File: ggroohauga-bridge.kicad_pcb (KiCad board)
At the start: 2 copper layers, 101.6 x 31 mm, 6 parts

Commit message: Move stuff around
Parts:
- moved C-Q1 6.23 mm to (135.7, 59.4)
- moved A-R1 4.06 mm to (74.7, 73.2)
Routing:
- net /GPIO_L40_C40_M41/CON_POWER_OUT: track 32.1 -> 38.5 mm
- net /CON_POWER_OUT: track 18.1 -> 11.9 mm
- net +3.3V: track 64.4 -> 70.6 mm
- net /AMP_POWER_IN: track 18.3 -> 14.0 mm
- net /GPIO_L8_C8_M10/AMP_POWER_IN: track 31.7 -> 36.0 mm
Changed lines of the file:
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@@
 	(footprint "Package_TO_SOT_SMD:SOT-23"
 		(layer "F.Cu")
-		(at 129.474 59.3575 -90)
+		(at 135.702 59.3575 -90)
 		(descr "SOT, 3 Pin (JEDEC TO-236 Var AB https://www.jedec.org/document_search?search_api_views_fulltext=TO-236), generated with kicad-footprint-generator ipc_gullwing_generator.py")
 		(tags "SOT TO_SOT_SMD")
 		(property "Reference" "C-Q1"
-			(at 1.0945 3.998 180)
+			(at -2.9695 0.066 180)
 			(layer "F.SilkS")
 			(effects
@@
 	(footprint "Resistor_SMD:R_0805_2012Metric_Pad1.20x1.40mm_HandSolder"
 		(layer "F.Cu")
-		(at 78.724 72.644 180)
+		(at 74.692 73.152 180)
 		(descr "Resistor SMD 0805 (2012 Metric), square (rectangular) end terminal, IPC_7351 nominal with elongated pad for handsoldering. (Body size source: IPC-SM-782 page 72, https://www.pcb-3d.com/wordpress/wp-content/uploads/ipc-sm-782a_amendment_1_and_2.pdf), generated with kicad-footprint-generator")
 		(tags "resistor handsolder")
@@
 	)
 	(segment
-		(start 74.168 73.66)
-		(end 63.5 73.66)
+		(start 62.8396 72.9996)
+		(end 62.8396 70.3192)
 		(width 0.2)
 		(layer "F.Cu")
@@
 	)
 	(segment
-		(start 77.724 72.644)
-		(end 75.184 72.644)
+		(start 71.12 73.152)
+		(end 73.692 73.152)
 		(width 0.2)
 		(layer "F.Cu")
@@
 	)
 	(segment
-		(start 75.184 72.644)
-		(end 74.168 73.66)
+		(start 63.5 73.66)
+		(end 70.612 73.66)
 		(width 0.2)
 		(layer "F.Cu")
@@
 	)
 	(segment
-		(start 62.8396 72.9996)
-		(end 62.8396 70.3192)
+		(start 63.5 73.66)
+		(end 62.8396 72.9996)
 		(width 0.2)
 		(layer "F.Cu")
@@
 	)
 	(segment
-		(start 63.5 73.66)
-		(end 62.8396 72.9996)
+		(start 70.612 73.66)
+		(end 71.12 73.152)
 		(width 0.2)
 		(layer "F.Cu")
@@
 	)
 	(segment
+		(start 79.724 72.644)
+		(end 79.216 73.152)
+		(width 0.2)
+		(layer "F.Cu")
+		(net 16)
+	)
+	(segment
 		(start 109.474 77.47)
 		(end 106.172 74.168)
@@
 	)
 	(segment
+		(start 79.216 73.152)
+		(end 75.692 73.152)
+		(width 0.2)
+		(layer "F.Cu")
+		(net 16)
+	)
+	(segment
 		(start 106.172 74.168)
 		(end 96.774 74.168)
@@
 	)
 	(segment
-		(start 124.46 72.644)
-		(end 129.474 72.644)
+		(start 135.636 72.644)
+		(end 124.46 72.644)
 		(width 0.2)
 		(layer "F.Cu")
@@
 	)
 	(segment
-		(start 83.312 73.66)
-		(end 81.788 73.66)
+		(start 135.702 60.295)
+		(end 135.702 72.578)
 		(width 0.2)
 		(layer "F.Cu")
@@
 	)
 	(segment
-		(start 81.534 73.914)
-		(end 81.534 77.47)
+		(start 135.702 72.578)
+		(end 135.636 72.644)
+		(width 0.2)
+		(layer "F.Cu")
+		(net 21)
+	)
+	(segment
+		(start 83.312 73.66)
+		(end 81.788 73.66)
 		(width 0.2)
 		(layer "F.Cu")
@@
 	)
 	(segment
-		(start 129.474 72.644)
-		(end 129.474 60.295)
+		(start 81.534 73.914)
+		(end 81.534 77.47)
 		(width 0.2)
 		(layer "F.Cu")
@@
 	)
 	(segment
-		(start 123.952 57.912)
-		(end 124.018 57.978)
-		(width 0.2)
-		(layer "F.Cu")
-		(net 22)
-	)
-	(segment
-		(start 124.018 57.978)
-		(end 128.524 57.978)
+		(start 124.46 58.42)
+		(end 134.752 58.42)
 		(width 0.2)
 		(layer "F.Cu")
@@
 	)
 	(via
-		(at 123.952 57.912)
+		(at 124.46 58.42)
 		(size 0.6)
 		(drill 0.3)
@@
 	)
 	(segment
-		(start 99.314 57.15)
-		(end 99.314 54.61)
+		(start 99.568 57.404)
+		(end 99.314 57.15)
 		(width 0.2)
 		(layer "B.Cu")
@@
 	)
 	(segment
-		(start 99.568 57.404)
-		(end 99.314 57.15)
+		(start 124.46 58.42)
+		(end 123.444 57.404)
 		(width 0.2)
 		(layer "B.Cu")
@@
 	)
 	(segment
-		(start 123.952 57.912)
-		(end 123.444 57.404)
+		(start 99.314 57.15)
+		(end 99.314 54.61)
 		(width 0.2)
 		(layer "B.Cu")
@@
 	(segment
 		(start 144.487759 58.42)
-		(end 146.5072 60.439441)
+		(end 136.652 58.42)
 		(width 0.2)
 		(layer "F.Cu")
@@
 	)
 	(segment
-		(start 130.424 58.42)
-		(end 144.487759 58.42)
+		(start 146.5072 61.6592)
+		(end 146.5072 60.439441)
 		(width 0.2)
 		(layer "F.Cu")
@@
 	(segment
 		(start 146.5072 60.439441)
-		(end 146.5072 61.6592)
+		(end 144.487759 58.42)
 		(width 0.2)
 		(layer "F.Cu")

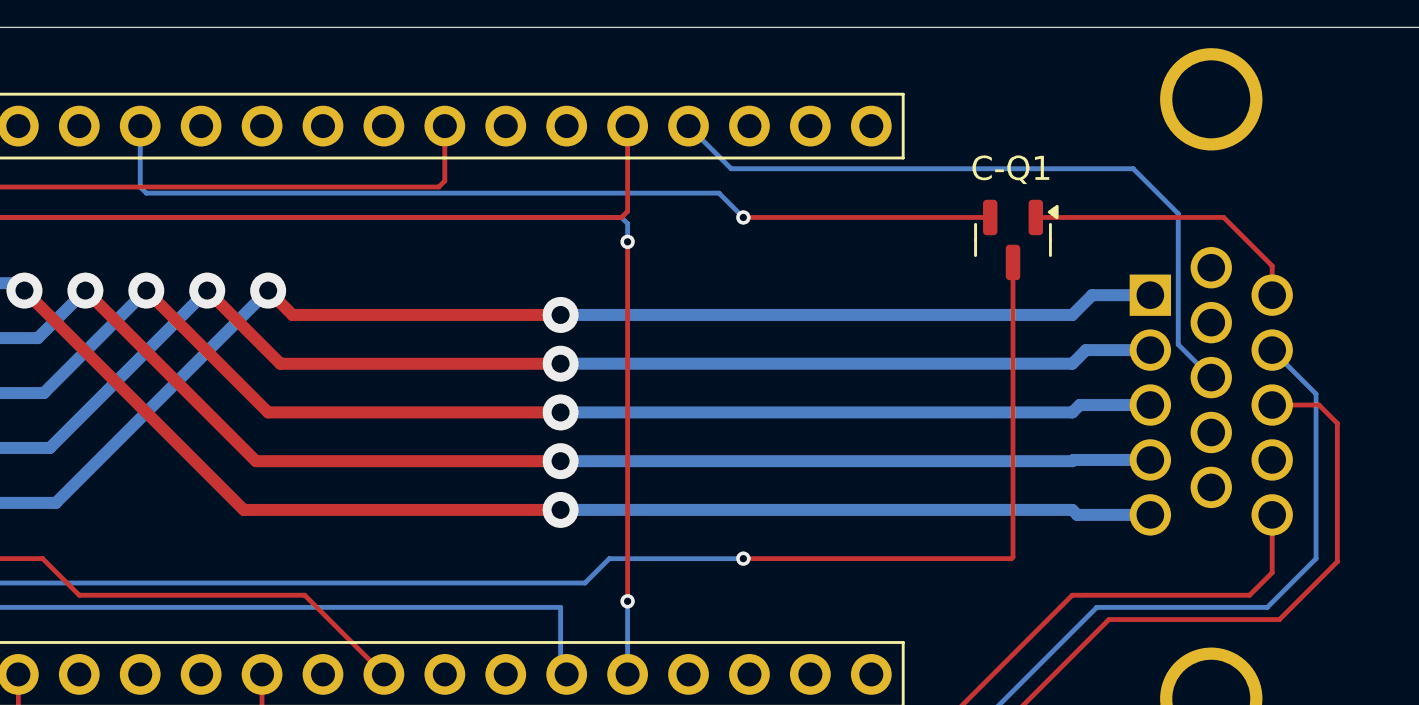
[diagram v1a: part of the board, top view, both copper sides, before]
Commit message: Rotate MOSFET pins so that it's connected correctly
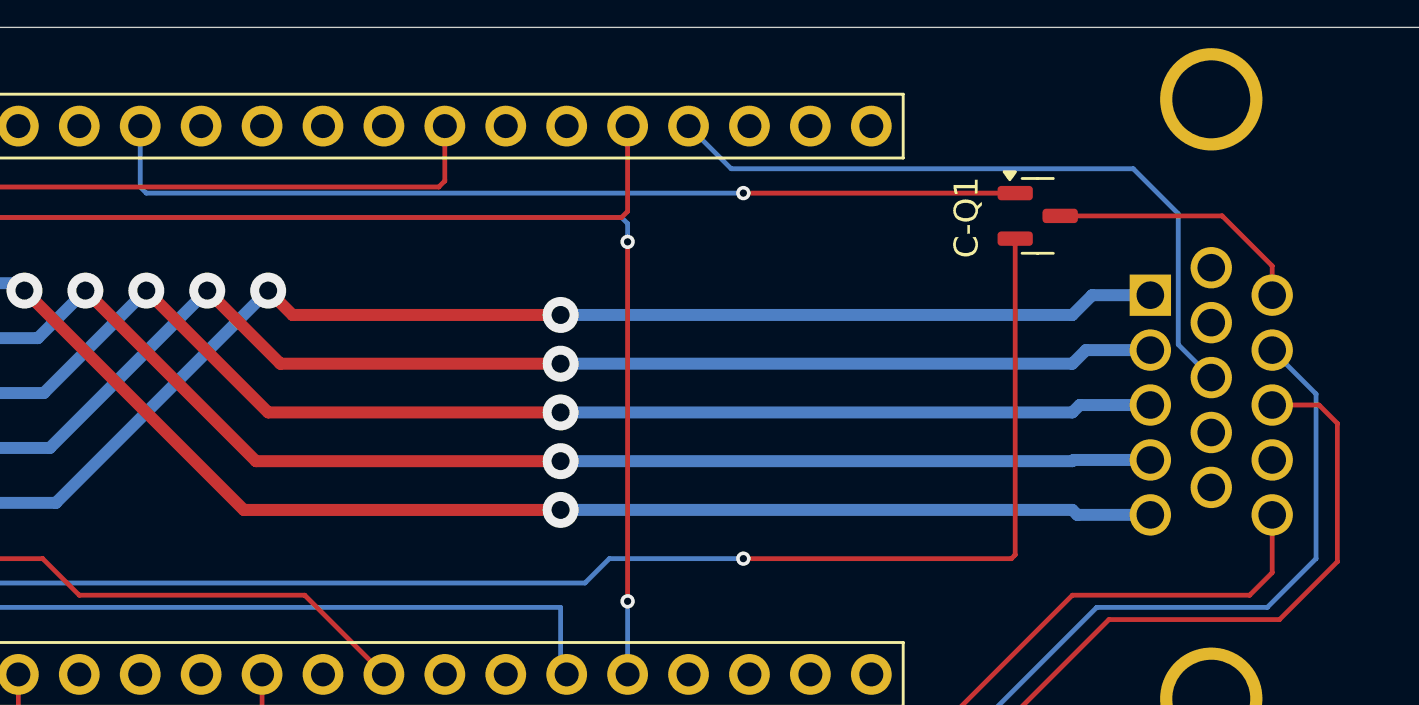
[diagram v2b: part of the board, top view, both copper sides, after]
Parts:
- moved C-Q1 1.44 mm to (136.7, 58.4), turned to 0 degrees
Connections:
- A-J1 pad S1: (no net) -> GND
- A-J1 pad S2: (no net) -> GND
- C-J1 pad SH1: (no net) -> GND
- C-J1 pad SH2: (no net) -> GND
- C-Q1 pad 1: /CON_POWER_OUT -> /GPIO_L40_C40_M41/CON_POWER_OUT
- C-Q1 pad 2: /GPIO_L40_C40_M41/CON_POWER_OUT -> +3.3V
- C-Q1 pad 3: +3.3V -> /CON_POWER_OUT
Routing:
- net +3.3V: track 70.6 -> 71.6 mm
- net /CON_POWER_OUT: track 11.9 -> 10.9 mm
- net /GPIO_L40_C40_M41/CON_POWER_OUT: track 38.5 -> 39.1 mm
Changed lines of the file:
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@@
 	(footprint "Package_TO_SOT_SMD:SOT-23"
 		(layer "F.Cu")
-		(at 135.702 59.3575 -90)
+		(at 136.7305 58.354)
 		(descr "SOT, 3 Pin (JEDEC TO-236 Var AB https://www.jedec.org/document_search?search_api_views_fulltext=TO-236), generated with kicad-footprint-generator ipc_gullwing_generator.py")
 		(tags "SOT TO_SOT_SMD")
 		(property "Reference" "C-Q1"
-			(at -2.9695 0.066 180)
+			(at -2.9695 0.066 90)
 			(layer "F.SilkS")
 			(effects
@@
 		)
 		(property "Value" "DMP2004K"
-			(at 0 2.4 90)
+			(at 0 2.4 0)
 			(layer "F.Fab")
 			(effects
@@
 		)
 		(property "Footprint" "Package_TO_SOT_SMD:SOT-23"
-			(at 0 0 90)
+			(at 0 0 0)
 			(layer "F.Fab")
 			(hide yes)
@@
 		)
 		(property "Datasheet" "https://www.diodes.com/assets/Datasheets/DMP2004K.pdf"
-			(at 0 0 90)
+			(at 0 0 0)
 			(layer "F.Fab")
 			(hide yes)
@@
 		)
 		(property "Description" "-600mA Id, -20V Vds, P-Channel MOSFET, SOT-23"
-			(at 0 0 90)
+			(at 0 0 0)
 			(layer "F.Fab")
 			(hide yes)
@@
 		)
 		(property "Sim.Device" "PMOS"
-			(at 0 0 -90)
+			(at 0 0 0)
 			(unlocked yes)
 			(layer "F.Fab")
@@
 		)
 		(property "Sim.Type" "VDMOS"
-			(at 0 0 -90)
+			(at 0 0 0)
 			(unlocked yes)
 			(layer "F.Fab")
@@
 			)
 		)
-		(property "Sim.Pins" "1=D 2=G 3=S"
-			(at 0 0 -90)
+		(property "Sim.Pins" "1=G 2=S 3=D"
+			(at 0 0 0)
 			(unlocked yes)
 			(layer "F.Fab")
@@
 		(attr smd)
 		(fp_line
-			(start 0 1.56)
-			(end -0.65 1.56)
+			(start 0 -1.56)
+			(end -0.65 -1.56)
 			(stroke
 				(width 0.12)
@@
 		)
 		(fp_line
-			(start 0 1.56)
-			(end 0.65 1.56)
+			(start 0 -1.56)
+			(end 0.65 -1.56)
 			(stroke
 				(width 0.12)
@@
 		)
 		(fp_line
-			(start 0 -1.56)
-			(end -0.65 -1.56)
+			(start 0 1.56)
+			(end -0.65 1.56)
 			(stroke
 				(width 0.12)
@@
 		)
 		(fp_line
-			(start 0 -1.56)
-			(end 0.65 -1.56)
+			(start 0 1.56)
+			(end 0.65 1.56)
 			(stroke
 				(width 0.12)
@@
 		)
 		(fp_line
-			(start -1.92 1.7)
-			(end 1.92 1.7)
+			(start -1.92 -1.7)
+			(end -1.92 1.7)
 			(stroke
 				(width 0.05)
@@
 		)
 		(fp_line
-			(start 1.92 1.7)
-			(end 1.92 -1.7)
+			(start -1.92 1.7)
+			(end 1.92 1.7)
 			(stroke
 				(width 0.05)
@@
 		)
 		(fp_line
-			(start -1.92 -1.7)
-			(end -1.92 1.7)
+			(start 1.92 -1.7)
+			(end -1.92 -1.7)
 			(stroke
 				(width 0.05)
@@
 		)
 		(fp_line
-			(start 1.92 -1.7)
-			(end -1.92 -1.7)
+			(start 1.92 1.7)
+			(end 1.92 -1.7)
 			(stroke
 				(width 0.05)
@@
 		)
 		(fp_line
-			(start -0.65 1.45)
-			(end -0.65 -1.125)
+			(start -0.65 -1.125)
+			(end -0.325 -1.45)
 			(stroke
 				(width 0.1)
@@
 		)
 		(fp_line
-			(start 0.65 1.45)
-			(end -0.65 1.45)
+			(start -0.65 1.45)
+			(end -0.65 -1.125)
 			(stroke
 				(width 0.1)
@@
 		)
 		(fp_line
-			(start -0.65 -1.125)
-			(end -0.325 -1.45)
+			(start -0.325 -1.45)
+			(end 0.65 -1.45)
 			(stroke
 				(width 0.1)
@@
 		)
 		(fp_line
-			(start -0.325 -1.45)
-			(end 0.65 -1.45)
+			(start 0.65 -1.45)
+			(end 0.65 1.45)
 			(stroke
 				(width 0.1)
@@
 		)
 		(fp_line
-			(start 0.65 -1.45)
-			(end 0.65 1.45)
+			(start 0.65 1.45)
+			(end -0.65 1.45)
 			(stroke
 				(width 0.1)
@@
 		)
 		(fp_text user "${REFERENCE}"
-			(at 0 0 90)
+			(at 0 0 0)
 			(layer "F.Fab")
 			(effects
@@
 		)
 		(pad "1" smd roundrect
-			(at -0.9375 -0.95 270)
+			(at -0.9375 -0.95)
 			(size 1.475 0.6)
 			(layers "F.Cu" "F.Paste" "F.Mask")
 			(roundrect_rratio 0.25)
-			(net 52 "/CON_POWER_OUT")
-			(pinfunction "D")
-			(pintype "passive")
+			(net 22 "/GPIO_L40_C40_M41{slash}CON_POWER_OUT")
+			(pinfunction "G")
+			(pintype "input")
 		)
 		(pad "2" smd roundrect
-			(at -0.9375 0.95 270)
+			(at -0.9375 0.95)
 			(size 1.475 0.6)
 			(layers "F.Cu" "F.Paste" "F.Mask")
 			(roundrect_rratio 0.25)
-			(net 22 "/GPIO_L40_C40_M41{slash}CON_POWER_OUT")
-			(pinfunction "G")
-			(pintype "input")
+			(net 21 "+3.3V")
+			(pinfunction "S")
+			(pintype "passive")
 		)
 		(pad "3" smd roundrect
-			(at 0.9375 0 270)
+			(at 0.9375 0)
 			(size 1.475 0.6)
 			(layers "F.Cu" "F.Paste" "F.Mask")
 			(roundrect_rratio 0.25)
-			(net 21 "+3.3V")
-			(pinfunction "S")
+			(net 52 "/CON_POWER_OUT")
+			(pinfunction "D")
 			(pintype "passive")
 		)
@@
 			)
 			(remove_unused_layers no)
+			(net 10 "GND")
 			(solder_mask_margin 0.102)
 		)
@@
 			)
 			(remove_unused_layers no)
+			(net 10 "GND")
 			(solder_mask_margin 0.102)
 		)
@@
 			)
 			(remove_unused_layers no)
+			(net 10 "GND")
 			(solder_mask_margin 0.102)
 		)
@@
 			)
 			(remove_unused_layers no)
+			(net 10 "GND")
 			(solder_mask_margin 0.102)
 		)
@@
 	)
 	(segment
-		(start 135.636 72.644)
-		(end 124.46 72.644)
+		(start 135.793 72.487)
+		(end 135.793 59.304)
 		(width 0.2)
 		(layer "F.Cu")
@@
 	)
 	(segment
-		(start 135.702 60.295)
-		(end 135.702 72.578)
+		(start 124.46 72.644)
+		(end 135.636 72.644)
 		(width 0.2)
 		(layer "F.Cu")
@@
 	)
 	(segment
-		(start 135.702 72.578)
-		(end 135.636 72.644)
+		(start 83.312 73.66)
+		(end 81.788 73.66)
 		(width 0.2)
 		(layer "F.Cu")
@@
 	)
 	(segment
-		(start 83.312 73.66)
-		(end 81.788 73.66)
+		(start 135.636 72.644)
+		(end 135.793 72.487)
 		(width 0.2)
 		(layer "F.Cu")
@@
 	)
 	(segment
-		(start 124.46 58.42)
-		(end 134.752 58.42)
+		(start 124.46 57.404)
+		(end 135.793 57.404)
 		(width 0.2)
 		(layer "F.Cu")
@@
 	)
 	(via
-		(at 124.46 58.42)
+		(at 124.46 57.404)
 		(size 0.6)
 		(drill 0.3)
@@
 	)
 	(segment
-		(start 99.568 57.404)
-		(end 99.314 57.15)
-		(width 0.2)
-		(layer "B.Cu")
-		(net 22)
-	)
-	(segment
-		(start 123.444 57.404)
-		(end 99.568 57.404)
+		(start 99.314 57.15)
+		(end 99.314 54.61)
 		(width 0.2)
 		(layer "B.Cu")
@@
 	)
 	(segment
-		(start 124.46 58.42)
-		(end 123.444 57.404)
+		(start 99.568 57.404)
+		(end 99.314 57.15)
 		(width 0.2)
 		(layer "B.Cu")
@@
 	)
 	(segment
-		(start 99.314 57.15)
-		(end 99.314 54.61)
+		(start 124.46 57.404)
+		(end 99.568 57.404)
 		(width 0.2)
 		(layer "B.Cu")
@@
 	)
 	(segment
-		(start 144.487759 58.42)
-		(end 136.652 58.42)
+		(start 137.668 58.354)
+		(end 144.421759 58.354)
 		(width 0.2)
 		(layer "F.Cu")
@@
 	)
 	(segment
-		(start 146.5072 61.6592)
-		(end 146.5072 60.439441)
+		(start 146.5072 60.439441)
+		(end 146.5072 61.6592)
 		(width 0.2)
 		(layer "F.Cu")
@@
 	)
 	(segment
-		(start 146.5072 60.439441)
-		(end 144.487759 58.42)
+		(start 144.421759 58.354)
+		(end 146.5072 60.439441)
 		(width 0.2)
 		(layer "F.Cu")

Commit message: Cleanup tracks
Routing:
- net GND: track 0.76 -> 0.00 mm
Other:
- board text added: "urn:oid:1.3.6.1.4.1.39777.1.3.1.3.2 https://github.com/nomis/ggroohauga-pcb (bridge)"
- board text removed: "urn:oid:1.3.6.1.4.1.39777.1.3.1.3.1 https://github.com/nomis/ggroohauga-pcb (bridge)"
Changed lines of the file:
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@@
 		)
 	)
-	(gr_text "urn:oid:1.3.6.1.4.1.39777.1.3.1.3.1\nhttps://github.com/nomis/ggroohauga-pcb\n(bridge)\n"
+	(gr_text "urn:oid:1.3.6.1.4.1.39777.1.3.1.3.2\nhttps://github.com/nomis/ggroohauga-pcb\n(bridge)\n"
 		(at 131.064 66.04 0)
 		(layer "B.SilkS")
@@
 	(segment
 		(start 112.014 54.61)
-		(end 111.76 54.61)
-		(width 0.2)
-		(layer "F.Cu")
-		(net 4)
-	)
-	(segment
-		(start 112.014 54.61)
 		(end 112.014 56.896)
 		(width 0.2)
@@
 	)
 	(segment
-		(start 62.84825 68.035)
-		(end 62.84825 67.96175)
-		(width 0.2)
-		(layer "F.Cu")
-		(net 7)
-	)
-	(segment
 		(start 116.84 74.676)
 		(end 59.69 74.676)
@@
 		(start 60.2408 68.0292)
 		(end 62.8396 68.0292)
-		(width 0.2)
-		(layer "B.Cu")
-		(net 7)
-	)
-	(segment
-		(start 117.094 77.47)
-		(end 116.84 77.47)
 		(width 0.2)
 		(layer "B.Cu")
@@
 	)
 	(segment
-		(start 65.38825 71.47)
-		(end 65.12 71.47)
-		(width 0.2)
-		(layer "F.Cu")
-		(net 10)
-	)
-	(segment
-		(start 65.12 71.47)
-		(end 64.77 71.12)
-		(width 0.2)
-		(layer "F.Cu")
-		(net 10)
-	)
-	(segment
 		(start 99.568 61.468)
 		(end 104.648 66.548)
@@
 	)
 	(segment
-		(start 146.4056 65.7374)
-		(end 146.4056 65.6336)
-		(width 0.2)
-		(layer "B.Cu")
-		(net 17)
-	)
-	(segment
-		(start 146.4056 65.6336)
-		(end 146.304 65.532)
-		(width 0.2)
-		(layer "B.Cu")
-		(net 17)
-	)
-	(segment
 		(start 146.304 74.676)
 		(end 148.336 72.644)
@@
 	)
 	(segment
-		(start 143.8656 66.9544)
-		(end 143.764 67.056)
-		(width 0.2)
-		(layer "F.Cu")
-		(net 50)
-	)
-	(segment
-		(start 143.8656 66.8824)
-		(end 143.8656 66.9544)
-		(width 0.2)
-		(layer "F.Cu")
-		(net 50)
-	)
-	(segment

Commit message: Convert to KiCad 9.0 format
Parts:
- A-J1: value DE15_Receptacle_HighDensity_MountingHoles -> DE15_Socket_HighDensity_MountingHoles
- C-J1: value DE15_Plug_HighDensity_MountingHoles -> DE15_Pins_HighDensity_MountingHoles

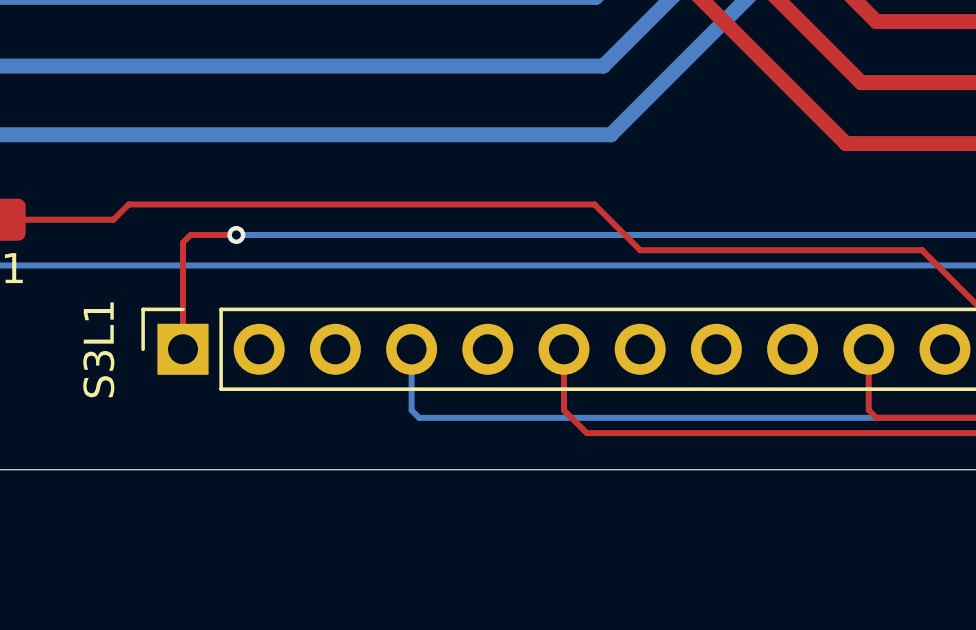
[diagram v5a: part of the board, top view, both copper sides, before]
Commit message: Reorganise schematic into multiple sheets and add 3 board identifier GPIOs
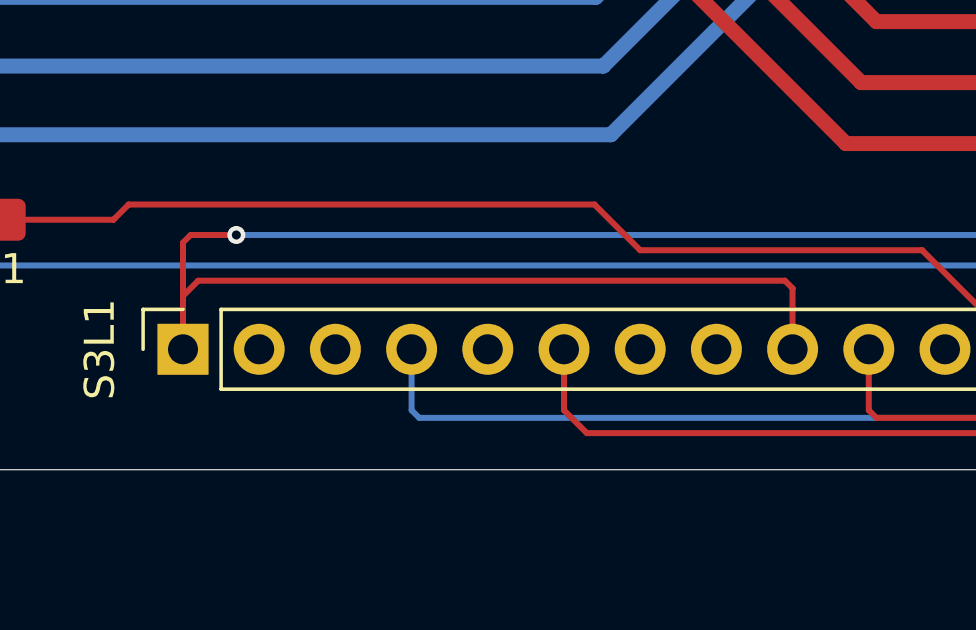
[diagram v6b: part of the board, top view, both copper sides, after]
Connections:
- net /AMP_POWER_IN renamed /Common/AMP_POWER_IN
- net /CON_POWER_OUT renamed /Common/CON_POWER_OUT
- net /GPIO_L13_C47_M26/AMP_ANNOUNCE renamed /Common/GPIO_L13_C47_M26/AMP_ANNOUNCE
- net /GPIO_L17_C17_M8/CON_DETECT renamed /Common/GPIO_L17_C17_M8/CON_DETECT
- net /GPIO_L40_C40_M41/CON_POWER_OUT renamed /Common/GPIO_L40_C40_M41/CON_POWER_OUT
- net /GPIO_L4_C4_M2/CON_RX renamed /Common/GPIO_L4_C4_M2/CON_RX
- net /GPIO_L6_C6_M4/CON_TX renamed /Common/GPIO_L6_C6_M4/CON_TX
- net /GPIO_L8_C8_M10/AMP_POWER_IN renamed /Common/GPIO_L8_C8_M10/AMP_POWER_IN
- A-J1 pad 12: /GPIO_L9_C9_M13/AMP_TX -> /Common/AMP_TX
- A-J1 pad 13: /GPIO_L10_C10_M14/AMP_RX -> /Common/AMP_RX
- A-J1 pad 15: /GPIO_L48_C35_M36/CON_ANNOUNCE -> /Common/CON_ANNOUNCE
- A-J1 pad 8: /GPIO_L14_C48_M33/AMP_DETECT -> /Common/AMP_DETECT
- S3L1 pad 11: unconnected-(S3L1-Pin_11-Pad11) -> GPIO_L18_C18_M9
- S3L1 pad 15: /GPIO_L9_C9_M13/AMP_TX -> /Common/GPIO_L9_C9_M13/AMP_TX
- S3L1 pad 16: /GPIO_L10_C10_M14/AMP_RX -> /Common/GPIO_L10_C10_M14/AMP_RX
- S3L1 pad 17: unconnected-(S3L1-Pin_17-Pad17) -> GPIO_L11_C11_M15
- S3L1 pad 18: unconnected-(S3L1-Pin_18-Pad18) -> GPIO_L12_C12_M16
- S3L1 pad 7: unconnected-(S3L1-Pin_7-Pad7) -> GND
- S3L1 pad 8: unconnected-(S3L1-Pin_8-Pad8) -> GND
- S3L1 pad 9: unconnected-(S3L1-Pin_9-Pad9) -> +3.3V
- S3R1 pad 13: /GPIO_L48_C35_M36/CON_ANNOUNCE -> /Common/GPIO_L48_C35_M36/CON_ANNOUNCE
- S3R1 pad 14: unconnected-(S3R1-Pin_14-Pad14) -> GPIO_L47_C47_M35
- S3R1 pad 15: unconnected-(S3R1-Pin_15-Pad15) -> GPIO_L21_C21_M21
- S3R1 pad 16: /GPIO_L14_C48_M33/AMP_DETECT -> /Common/GPIO_L14_C48_M33/AMP_DETECT
- S3R1 pad 7: unconnected-(S3R1-Pin_7-Pad7) -> GPIO_L41_C41_M42
- S3R1 pad 9: unconnected-(S3R1-Pin_9-Pad9) -> GPIO_L39_C39_M40
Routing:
- net (no net): track 0.00 -> 278.7 mm, vias 0 -> 2
- net /GPIO_L10_C10_M14/AMP_RX: track 88.8 -> 0.00 mm, vias 2 -> 0
- net /GPIO_L9_C9_M13/AMP_TX: track 69.4 -> 0.00 mm
- net /GPIO_L14_C48_M33/AMP_DETECT: track 65.2 -> 0.00 mm
- net /GPIO_L48_C35_M36/CON_ANNOUNCE: track 55.2 -> 0.00 mm
- net +3.3V: track 71.6 -> 96.0 mm
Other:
- board text added: "urn:oid:1.3.6.1.4.1.39777.1.3.1.3.3 https://github.com/nomis/ggroohauga-pcb (bridge)"
- board text removed: "urn:oid:1.3.6.1.4.1.39777.1.3.1.3.2 https://github.com/nomis/ggroohauga-pcb (bridge)"
